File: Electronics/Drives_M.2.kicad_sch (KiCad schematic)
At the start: 85 parts, among them IC2 LM61480Q3RPHRQ1, J10 Bus_M.2_Socket_M, J11 Bus_M.2_Socket_M, J12 Bus_M.2_Socket_M, J13 Bus_M.2_Socket_M, M1 M.2 Solder Nut, M10 M.2 Screw, M11 M.2 Solder Nut, M12 M.2 Solder Nut, M13 M.2 Solder Nut, M14 M.2 Solder Nut, M15 M.2 Screw, M16 M.2 Solder Nut, M17 M.2 Solder Nut, M18 M.2 Solder Nut, M19 M.2 Solder Nut, M2 M.2 Solder Nut, M20 M.2 Screw, M3 M.2 Solder Nut, M4 M.2 Solder Nut, M5 M.2 Screw, M6 M.2 Solder Nut, M7 M.2 Solder Nut, M8 M.2 Solder Nut, M9 M.2 Solder Nut, U10 ASEK-32.768KHZ-L-R-T, U9 ASM1184

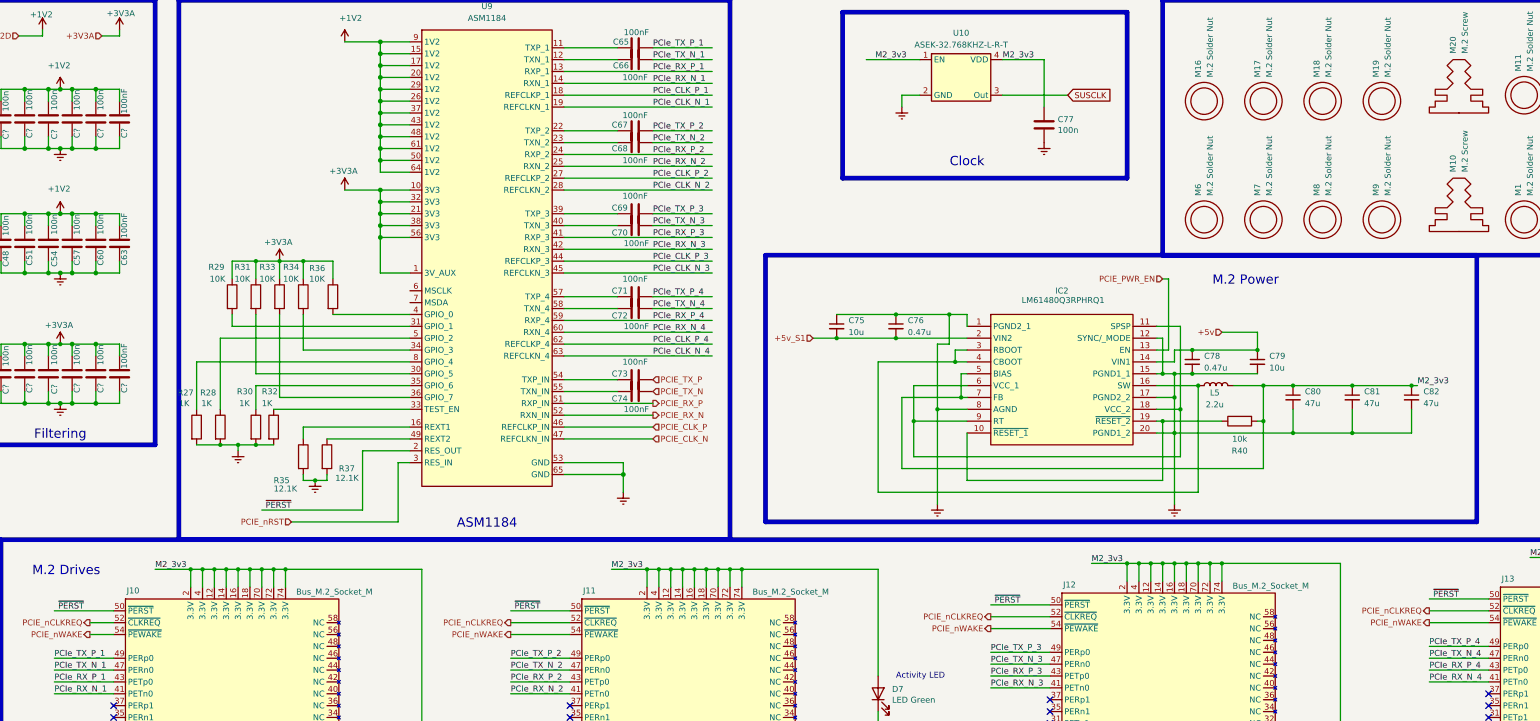
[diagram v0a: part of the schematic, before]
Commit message: Rp2040 Power Sequence finished and general cleaning
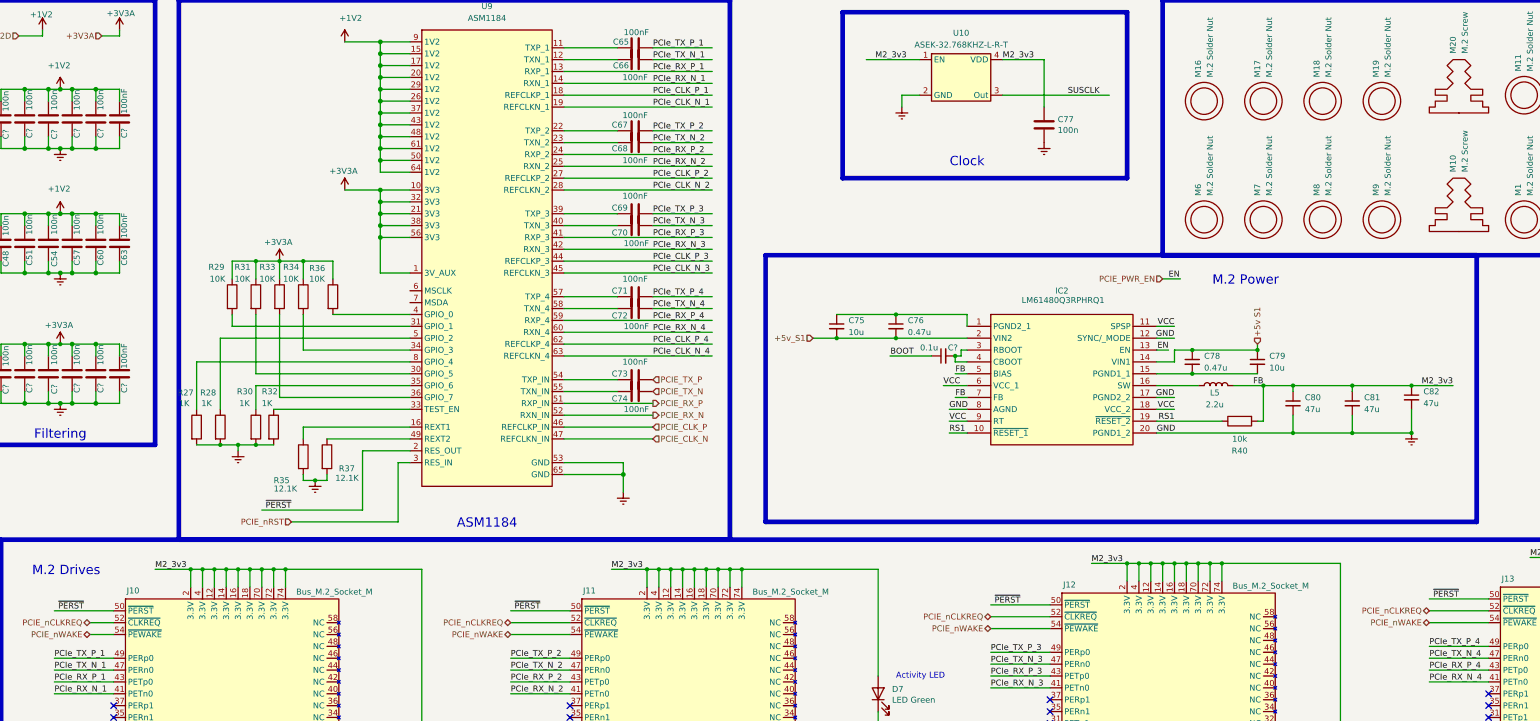
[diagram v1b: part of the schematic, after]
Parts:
- added C?: 0.1u, symbol Device:C_Small
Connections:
- net at IC2.16 (SW), L5.1: no longer IC2.3 (RBOOT), IC2.4 (CBOOT)
- net at C75.1, C76.1, IC2.1 (PGND2_1): no longer IC2.8 (AGND)
- net GND: now reaches C80.2, C81.2, C82.2, IC2.12 (SYNC/_MODE), IC2.17 (PGND2_2), IC2.20 (PGND1_2)
- net GND: now also IC2.8 (AGND); no longer C78.2, C79.2, IC2.15 (PGND1_1)
- net RS1: now reaches IC2.10 (~{RESET_1}), IC2.19 (~{RESET_2}), R40.1
- net VCC: now reaches IC2.11 (SPSP), IC2.18 (VCC_2), IC2.6 (VCC_1), IC2.9 (RT)
- net +5v renamed +5v S1
- net M2_3v3 renamed FB
- new net: C78.2, C79.2, IC2.15 (PGND1_1)
- new net: C?.2, IC2.3 (RBOOT), IC2.4 (CBOOT)
- new net BOOT: C?.1
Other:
- moved on the sheet: C80, C81

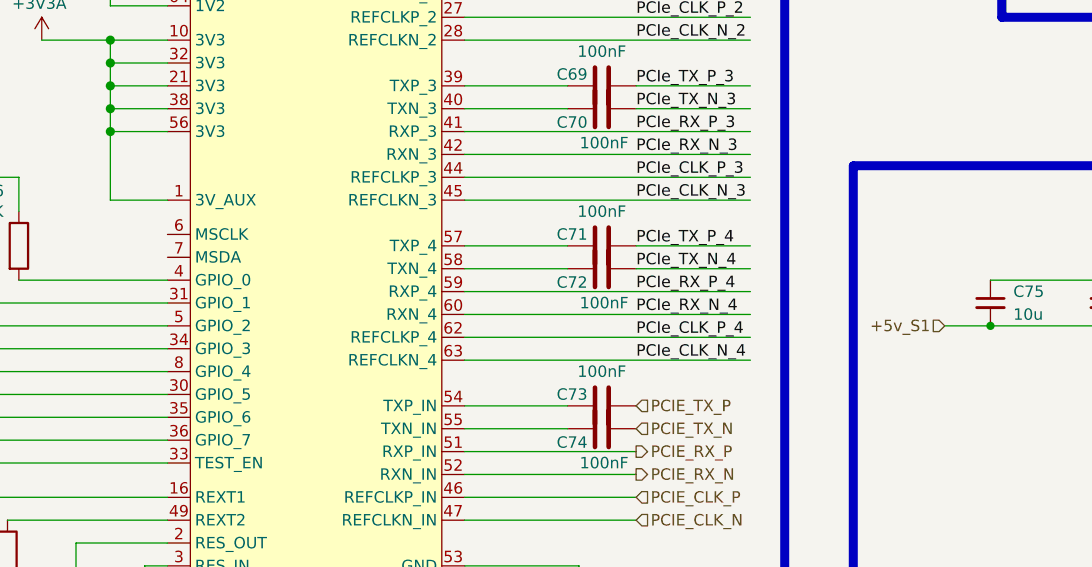
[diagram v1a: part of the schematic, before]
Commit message: Starting the Sheet connections
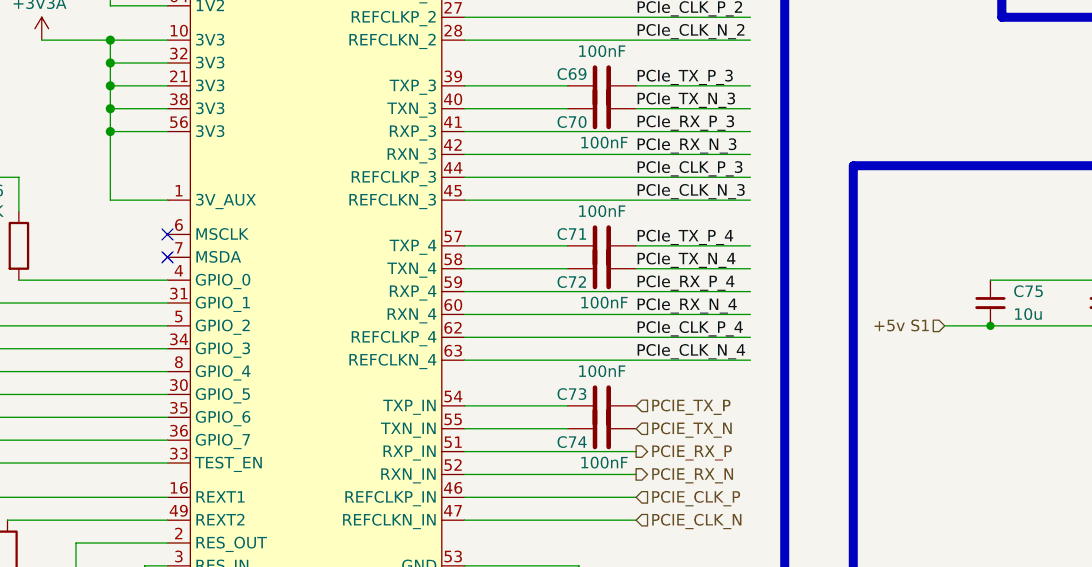
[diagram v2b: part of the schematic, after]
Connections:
- net +5v_S1 is gone; now on net +5v S1: C75.2, C76.2, IC2.2 (VIN2)
- no-connect marks 56 -> 58
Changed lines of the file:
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@@
 	)
 	(no_connect
+		(at 104.14 78.74)
+	)
+	(no_connect
 		(at 335.28 170.18)
 	)
@@
 	)
 	(no_connect
+		(at 104.14 76.2)
+	)
+	(no_connect
 		(at 241.3 191.77)
 	)
@@
 		)
 	)
-	(hierarchical_label "+5v_S1"
+	(hierarchical_label "+5v S1"
 		(shape input)
 		(at 190.5 86.36 180)

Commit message: Footprints Selected
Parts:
- C52, C54, C55, C57, C58, C60, C61, C63, C64, C66, C67, C69: renamed from C?; footprint Capacitor_SMD:C_0402_1005Metric -> Capacitor_SMD:C_0603_1608Metric
- C53: renamed from C48; footprint Capacitor_SMD:C_0402_1005Metric -> Capacitor_SMD:C_0603_1608Metric
- C56: renamed from C51; footprint Capacitor_SMD:C_0402_1005Metric -> Capacitor_SMD:C_0603_1608Metric
- C59: renamed from C54; footprint Capacitor_SMD:C_0402_1005Metric -> Capacitor_SMD:C_0603_1608Metric
- C62: renamed from C57; footprint Capacitor_SMD:C_0402_1005Metric -> Capacitor_SMD:C_0603_1608Metric
- C65: renamed from C60; footprint Capacitor_SMD:C_0402_1005Metric -> Capacitor_SMD:C_0603_1608Metric
- C68: renamed from C63; footprint Capacitor_SMD:C_0402_1005Metric -> Capacitor_SMD:C_0603_1608Metric
- C70: renamed from C65; footprint Capacitor_SMD:C_0402_1005Metric -> Capacitor_SMD:C_0603_1608Metric
- C71: renamed from C66; footprint Capacitor_SMD:C_0402_1005Metric -> Capacitor_SMD:C_0603_1608Metric
- C72: renamed from C67; footprint Capacitor_SMD:C_0402_1005Metric -> Capacitor_SMD:C_0603_1608Metric
- C73: renamed from C68; footprint Capacitor_SMD:C_0402_1005Metric -> Capacitor_SMD:C_0603_1608Metric
- C74: renamed from C69; footprint Capacitor_SMD:C_0402_1005Metric -> Capacitor_SMD:C_0603_1608Metric
- C75: renamed from C70; footprint Capacitor_SMD:C_0402_1005Metric -> Capacitor_SMD:C_0603_1608Metric
- C76: renamed from C71; footprint Capacitor_SMD:C_0402_1005Metric -> Capacitor_SMD:C_0603_1608Metric
- C77: renamed from C72; footprint Capacitor_SMD:C_0402_1005Metric -> Capacitor_SMD:C_0603_1608Metric
- C78: renamed from C73; footprint Capacitor_SMD:C_0402_1005Metric -> Capacitor_SMD:C_0603_1608Metric
- C79: renamed from C74; footprint Capacitor_SMD:C_0402_1005Metric -> Capacitor_SMD:C_0603_1608Metric
- C80: renamed from C75; footprint (none) -> Capacitor_SMD:C_0603_1608Metric
- C81: renamed from C76; footprint (none) -> Capacitor_SMD:C_0603_1608Metric
- C82: renamed from C?; footprint (none) -> Capacitor_SMD:C_0603_1608Metric
- C83: renamed from C77; footprint Capacitor_SMD:C_0402_1005Metric -> Capacitor_SMD:C_0603_1608Metric
- C84: renamed from C78; footprint (none) -> Capacitor_SMD:C_0603_1608Metric
- C85: renamed from C79; footprint (none) -> Capacitor_SMD:C_0603_1608Metric
- C86: renamed from C80; footprint (none) -> Capacitor_SMD:C_0603_1608Metric
- C87: renamed from C81; footprint (none) -> Capacitor_SMD:C_0603_1608Metric
- C88: renamed from C82; footprint (none) -> Capacitor_SMD:C_0603_1608Metric
- IC3: renamed from IC2; footprint LM62460QRPHRQ1 -> LIB_LM61480Q3RPHRQ1:LM62460QRPHRQ1
- J16: renamed from J10; footprint CM5IO:M.2 M Key socket -> 2199119-5:21991195
- J17: renamed from J11; footprint CM5IO:M.2 M Key socket -> 2199119-5:21991195
- J18: renamed from J12; footprint CM5IO:M.2 M Key socket -> 2199119-5:21991195
- J19: renamed from J13; footprint CM5IO:M.2 M Key socket -> 2199119-5:21991195
- L5: footprint (none) -> SRN5040-2R2Y:SRN50402R2Y
- R34: renamed from R27; footprint Resistor_SMD:R_0402_1005Metric -> Resistor_SMD:R_0603_1608Metric
- R35: renamed from R28; footprint Resistor_SMD:R_0402_1005Metric -> Resistor_SMD:R_0603_1608Metric
- R36: renamed from R29; footprint Resistor_SMD:R_0402_1005Metric -> Resistor_SMD:R_0603_1608Metric
- R37: renamed from R31; footprint Resistor_SMD:R_0402_1005Metric -> Resistor_SMD:R_0603_1608Metric
- R38: renamed from R30; footprint Resistor_SMD:R_0402_1005Metric -> Resistor_SMD:R_0603_1608Metric
- R39: renamed from R32; footprint Resistor_SMD:R_0402_1005Metric -> Resistor_SMD:R_0603_1608Metric
- R40: renamed from R33; footprint Resistor_SMD:R_0402_1005Metric -> Resistor_SMD:R_0603_1608Metric
- R41: renamed from R34; footprint Resistor_SMD:R_0402_1005Metric -> Resistor_SMD:R_0603_1608Metric
- R42: renamed from R35; footprint Resistor_SMD:R_0402_1005Metric -> Resistor_SMD:R_0603_1608Metric
- R43: renamed from R37; footprint Resistor_SMD:R_0402_1005Metric -> Resistor_SMD:R_0603_1608Metric
- R44: renamed from R36; footprint Resistor_SMD:R_0402_1005Metric -> Resistor_SMD:R_0603_1608Metric
- R45: renamed from R38; footprint Resistor_SMD:R_0402_1005Metric -> Resistor_SMD:R_0603_1608Metric
- R46: renamed from R39; footprint Resistor_SMD:R_0402_1005Metric -> Resistor_SMD:R_0603_1608Metric
- R47: renamed from R40; footprint (none) -> Resistor_SMD:R_0603_1608Metric
- R48: renamed from R41; footprint Resistor_SMD:R_0402_1005Metric -> Resistor_SMD:R_0603_1608Metric
- R49: renamed from R42; footprint Resistor_SMD:R_0402_1005Metric -> Resistor_SMD:R_0603_1608Metric
- TP10: renamed from TP4; footprint TestPoint:TestPoint_Pad_2.0x2.0mm -> TestPoint:TestPoint_Pad_1.0x1.0mm
- renumbered D6 to D12, D7 to D13, D8 to D14, D9 to D15, M16 to M1, M1 to M12, M12 to M13, M2 to M14, M13 to M15, M3 to M16, M14 to M17, M4 to M18, M15 to M19, M6 to M2, M5 to M20, M17 to M3, M7 to M4, M18 to M5, M8 to M6, M19 to M7, M9 to M8, M20 to M9, U9 to U7, U10 to U8
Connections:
- net +5v S1 renamed +5V S1

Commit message: Footprints selected, Hiracicle connections created, Pcb next
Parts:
- C52: renamed from C70; value 100nF -> 100n; footprint Capacitor_SMD:C_0603_1608Metric -> Capacitor_SMD:C_0402_1005Metric
- C53: renamed from C71; value 100nF -> 100n; footprint Capacitor_SMD:C_0603_1608Metric -> Capacitor_SMD:C_0402_1005Metric
- C59: renamed from C67; value 100nF -> 100n
- C60: renamed from C83; footprint Capacitor_SMD:C_0603_1608Metric -> Capacitor_SMD:C_0402_1005Metric
- C61: renamed from C72; value 100nF -> 100n; footprint Capacitor_SMD:C_0603_1608Metric -> Capacitor_SMD:C_0402_1005Metric
- C62: renamed from C73; value 100nF -> 100n; footprint Capacitor_SMD:C_0603_1608Metric -> Capacitor_SMD:C_0402_1005Metric
- C63: renamed from C74; value 100nF -> 100n; footprint Capacitor_SMD:C_0603_1608Metric -> Capacitor_SMD:C_0402_1005Metric
- C64: renamed from C75; value 100nF -> 100n; footprint Capacitor_SMD:C_0603_1608Metric -> Capacitor_SMD:C_0402_1005Metric
- C70: renamed from C68; value 100nF -> 100n
- C71: renamed from C76; value 100nF -> 100n; footprint Capacitor_SMD:C_0603_1608Metric -> Capacitor_SMD:C_0402_1005Metric
- C72: renamed from C77; value 100nF -> 100n; footprint Capacitor_SMD:C_0603_1608Metric -> Capacitor_SMD:C_0402_1005Metric
- C73: renamed from C80; footprint Capacitor_SMD:C_0603_1608Metric -> Capacitor_SMD:C_0805_2012Metric
- C74: renamed from C81; value 0.47u -> 0u47
- C75: renamed from C82; value 0.1u -> 100n; footprint Capacitor_SMD:C_0603_1608Metric -> Capacitor_SMD:C_0402_1005Metric
- C76: renamed from C84; value 0.47u -> 0u47
- C77: renamed from C85; footprint Capacitor_SMD:C_0603_1608Metric -> Capacitor_SMD:C_0805_2012Metric
- C83: renamed from C69; value 100nF -> 100n
- C84: renamed from C78; value 100nF -> 100n; footprint Capacitor_SMD:C_0603_1608Metric -> Capacitor_SMD:C_0402_1005Metric
- C85: renamed from C79; value 100nF -> 100n; footprint Capacitor_SMD:C_0603_1608Metric -> Capacitor_SMD:C_0402_1005Metric
- C86: renamed from C88; footprint Capacitor_SMD:C_0603_1608Metric -> Capacitor_SMD:C_0805_2012Metric
- C87: renamed from C86; footprint Capacitor_SMD:C_0603_1608Metric -> Capacitor_SMD:C_0805_2012Metric
- C88: renamed from C87; footprint Capacitor_SMD:C_0603_1608Metric -> Capacitor_SMD:C_0805_2012Metric
- L5: value 2.2u -> 2u2
- R42, R43: value 12.1K -> 12K1
- TP12: renamed from TP10; now not fitted
- renumbered C52 to C54, C58 to C56, C61 to C57, C64 to C58, C53 to C65, C56 to C66, C59 to C67, C62 to C68, C65 to C69, C54 to C78, C57 to C79, C60 to C80, C63 to C81, C66 to C82, D13 to D10, D15 to D11, D14 to D12, D12 to D13, J19 to J16, J18 to J17, J16 to J18, J17 to J19, M19 to M1, M7 to M10, M10 to M11, M20 to M12, M2 to M13, M4 to M14, M6 to M15, M8 to M16, M12 to M17, M14 to M18, M16 to M19, M9 to M2, M18 to M20, M11 to M3, M13 to M4, M15 to M5, M17 to M6, M1 to M7, M3 to M8, M5 to M9, R36 to R32, R37 to R33, R40 to R34, R41 to R35, R44 to R36, R47 to R37, R34 to R38, R35 to R39, R38 to R40, R39 to R41, R49 to R44, R48 to R45, R45 to R46, R46 to R47, U8 to U7, U7 to U8
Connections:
- net GND is gone; now on net gnd: C86.2, C87.2, C88.2, IC3.12 (SYNC/_MODE), IC3.17 (PGND2_2), IC3.20 (PGND1_2), IC3.8 (AGND)
- net gnd: now reaches R42.2, R43.2
- net gnd: now also C54.2, C55.2, C56.2, C57.2, C58.2, C59.2, C60.2, C65.2, C66.2, C67.2, C68.2, C69.2, C70.2, C78.2, C79.2, C80.2, C81.2, C82.2, C83.2, J16.1 (GND), J16.15 (GND), J16.21 (GND), J16.27 (GND), J16.3 (GND), J16.33 (GND), J16.39 (GND), J16.45 (GND), J16.51 (GND), J16.57 (GND), J16.71 (GND), J16.73 (GND), J16.75 (GND), J16.9 (GND), J16.M1 (GND2230), J16.M2 (GND2242), J16.M3 (GND2260), J16.M4 (GND2280), J16.S1, J16.S2, J17.1 (GND), J17.15 (GND), J17.21 (GND), J17.27 (GND), J17.3 (GND), J17.33 (GND), J17.39 (GND), J17.45 (GND), J17.51 (GND), J17.57 (GND), J17.71 (GND), J17.73 (GND), J17.75 (GND), J17.9 (GND), J17.M1 (GND2230), J17.M2 (GND2242), J17.M3 (GND2260), J17.M4 (GND2280), J17.S1, J17.S2, J18.1 (GND), J18.15 (GND), J18.21 (GND), J18.27 (GND), J18.3 (GND), J18.33 (GND), J18.39 (GND), J18.45 (GND), J18.51 (GND), J18.57 (GND), J18.71 (GND), J18.73 (GND), J18.75 (GND), J18.9 (GND), J18.M1 (GND2230), J18.M2 (GND2242), J18.M3 (GND2260), J18.M4 (GND2280), J18.S1, J18.S2, J19.1 (GND), J19.15 (GND), J19.21 (GND), J19.27 (GND), J19.3 (GND), J19.33 (GND), J19.39 (GND), J19.45 (GND), J19.51 (GND), J19.57 (GND), J19.71 (GND), J19.73 (GND), J19.75 (GND), J19.9 (GND), J19.M1 (GND2230), J19.M2 (GND2242), J19.M3 (GND2260), J19.M4 (GND2280), J19.S1, J19.S2, R38.2, R39.2, R40.2, R41.2, U7.2 (GND), U8.53 (GND), U8.65 (GND)
- net ~{PERST} renamed gnd{PERST}

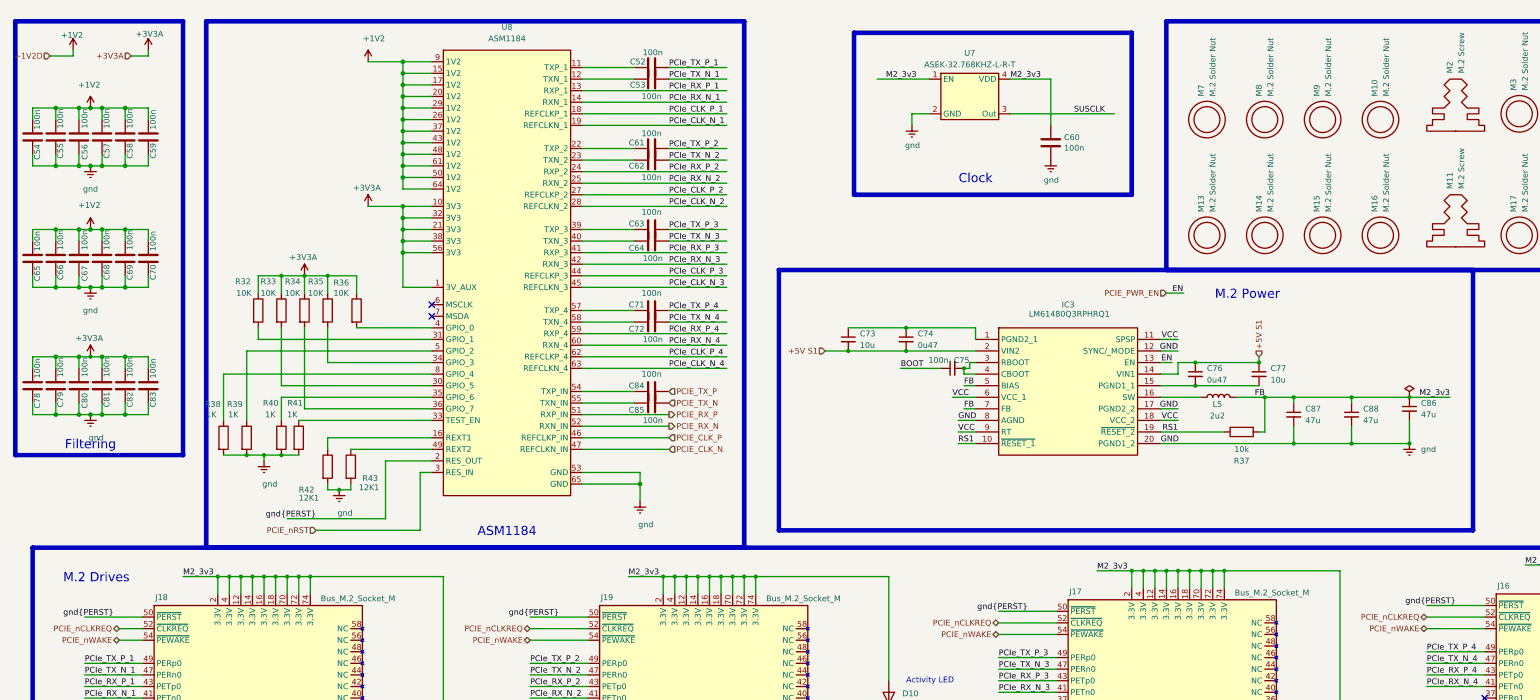
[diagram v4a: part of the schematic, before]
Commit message: Sata Port Changed
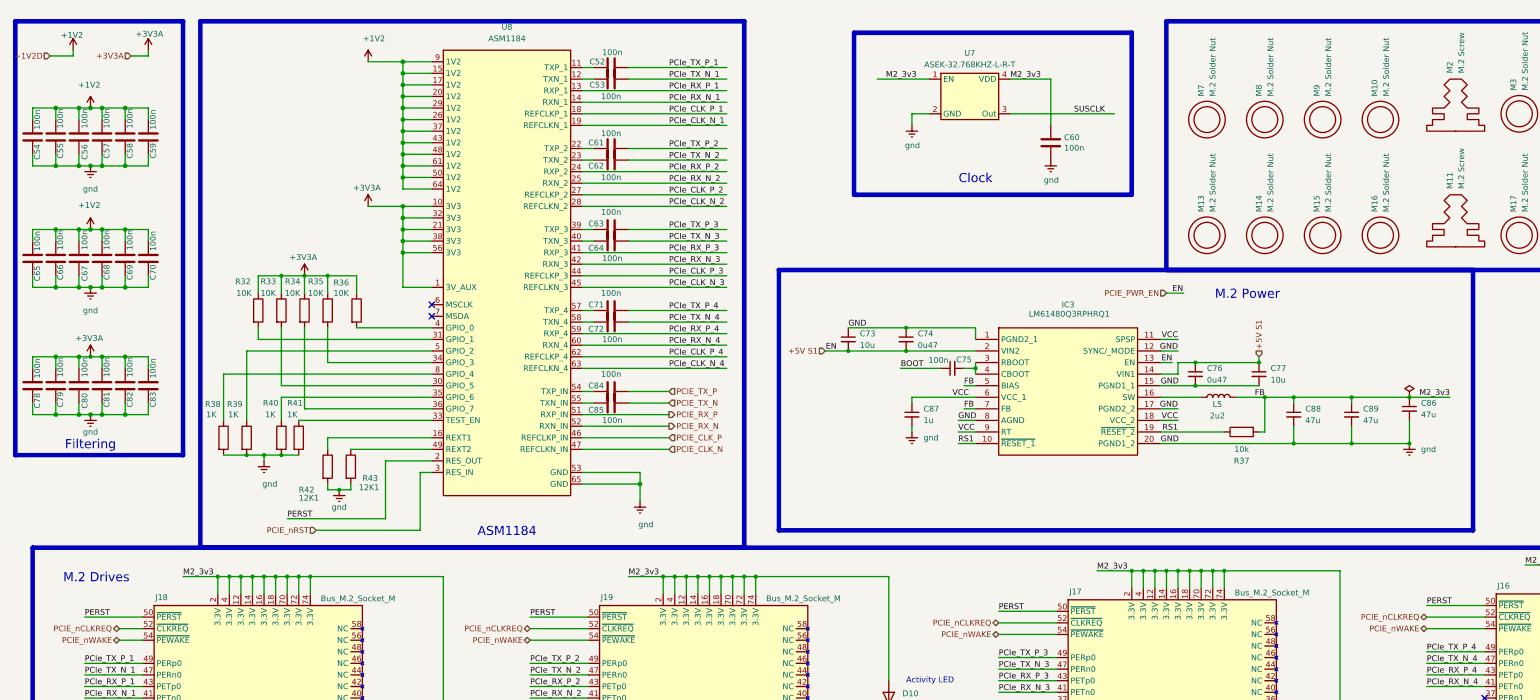
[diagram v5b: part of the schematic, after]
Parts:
- added C87: 1u, Capacitor_SMD:C_0805_2012Metric, symbol Device:C_Small
- J16, J17, J18, J19: footprint 2199119-5:21991195 -> M.2 M Key socket:M.2 M Key socket
- renumbered C87 to C88, C88 to C89
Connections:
- net PCIE_PWR_EN is gone; now on net +5V S1: IC3.13 (EN)
- net VCC: now also C87.1
- net gnd: now also C73.1, C74.1, C76.2, C77.2, IC3.1 (PGND2_1), IC3.15 (PGND1_1), C87.2
- net gnd{PERST} renamed PERST
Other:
- moved on the sheet: C52, C53, C61, C62, C63, C64, C71, C72, C84, C85
